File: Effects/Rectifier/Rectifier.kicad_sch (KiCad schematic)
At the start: 36 parts, among them J1 Conn_02x04_Odd_Even, J2 Conn_02x04_Odd_Even, SW1 SW_SPDT, U1 OPA1656, U2 BUF634AxD, U3 OPA1656

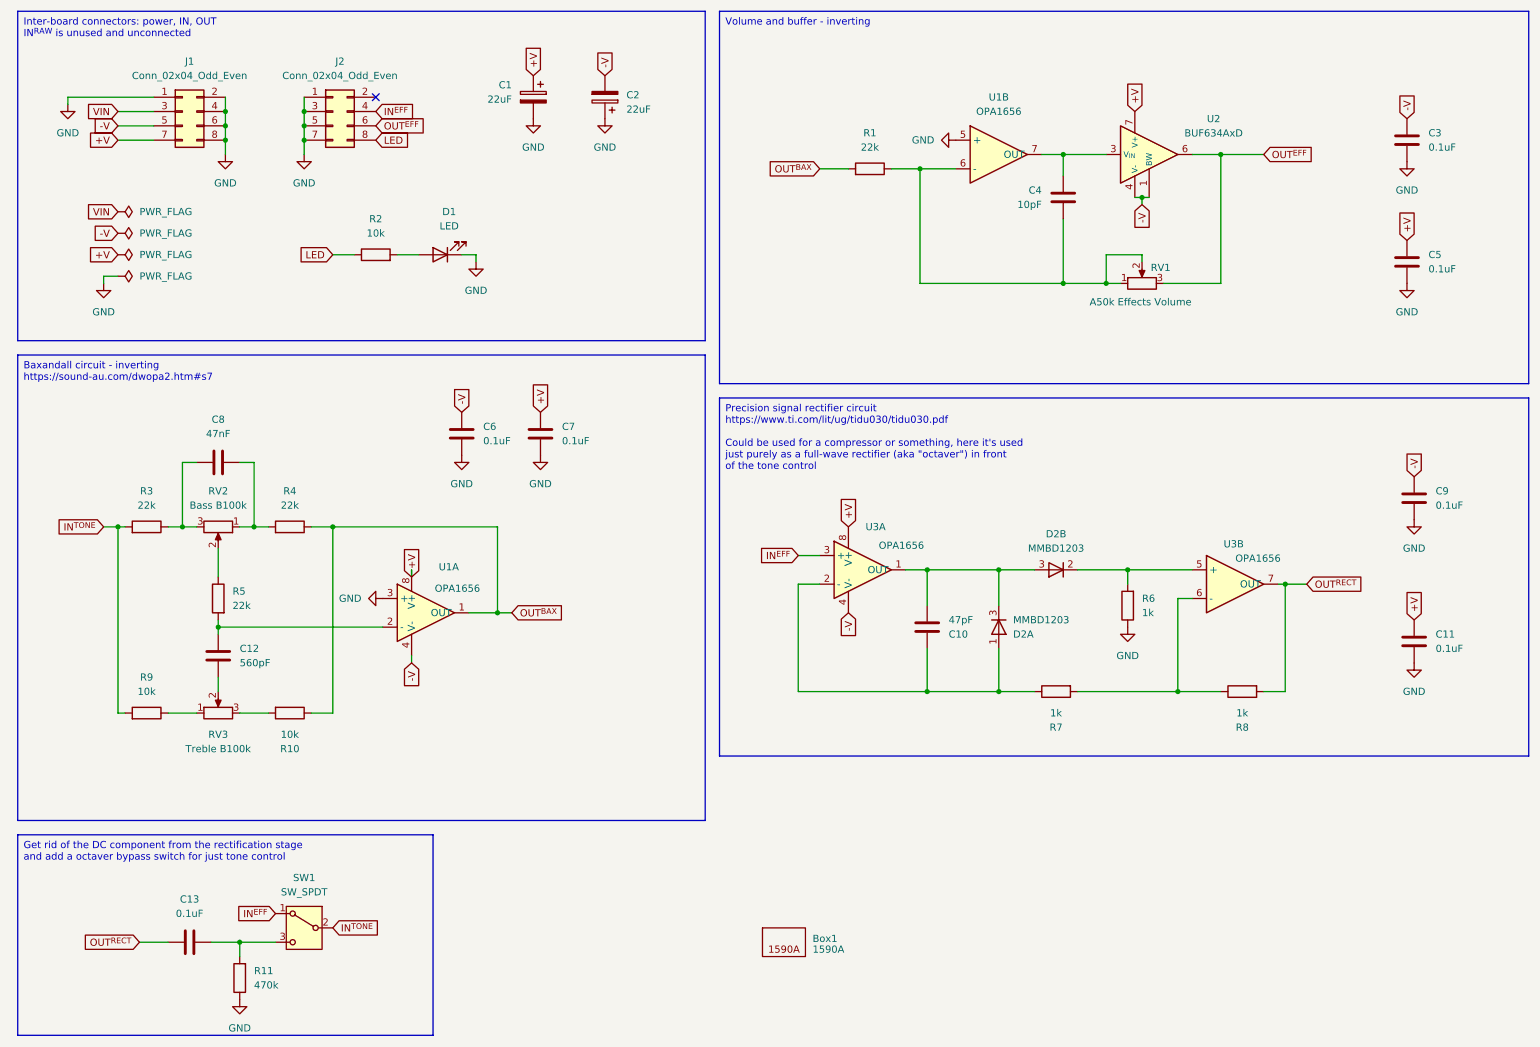
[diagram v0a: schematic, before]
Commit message: Octaver: replace the effect switch with a blending pot
Instead of a hard switch between octaver circuit bypass, use a pot and
another op-amp to blend the original and the rectified signal before the
tone control.

To make it all simpler, this removes the DC bias after blending, so that
the blending inputs are both driven similarly directly from the previous
op-amp.

It shouldn't matter - the blending stage will happily blend in the DC
offset and while it conceptually makes more sense after the
rectification stage rather than the blending stage, the end result is
the same.

Let's hope the end result is "it works". That would be good.

Signed-off-by: Linus Torvalds <torvalds@linux-foundation.org>
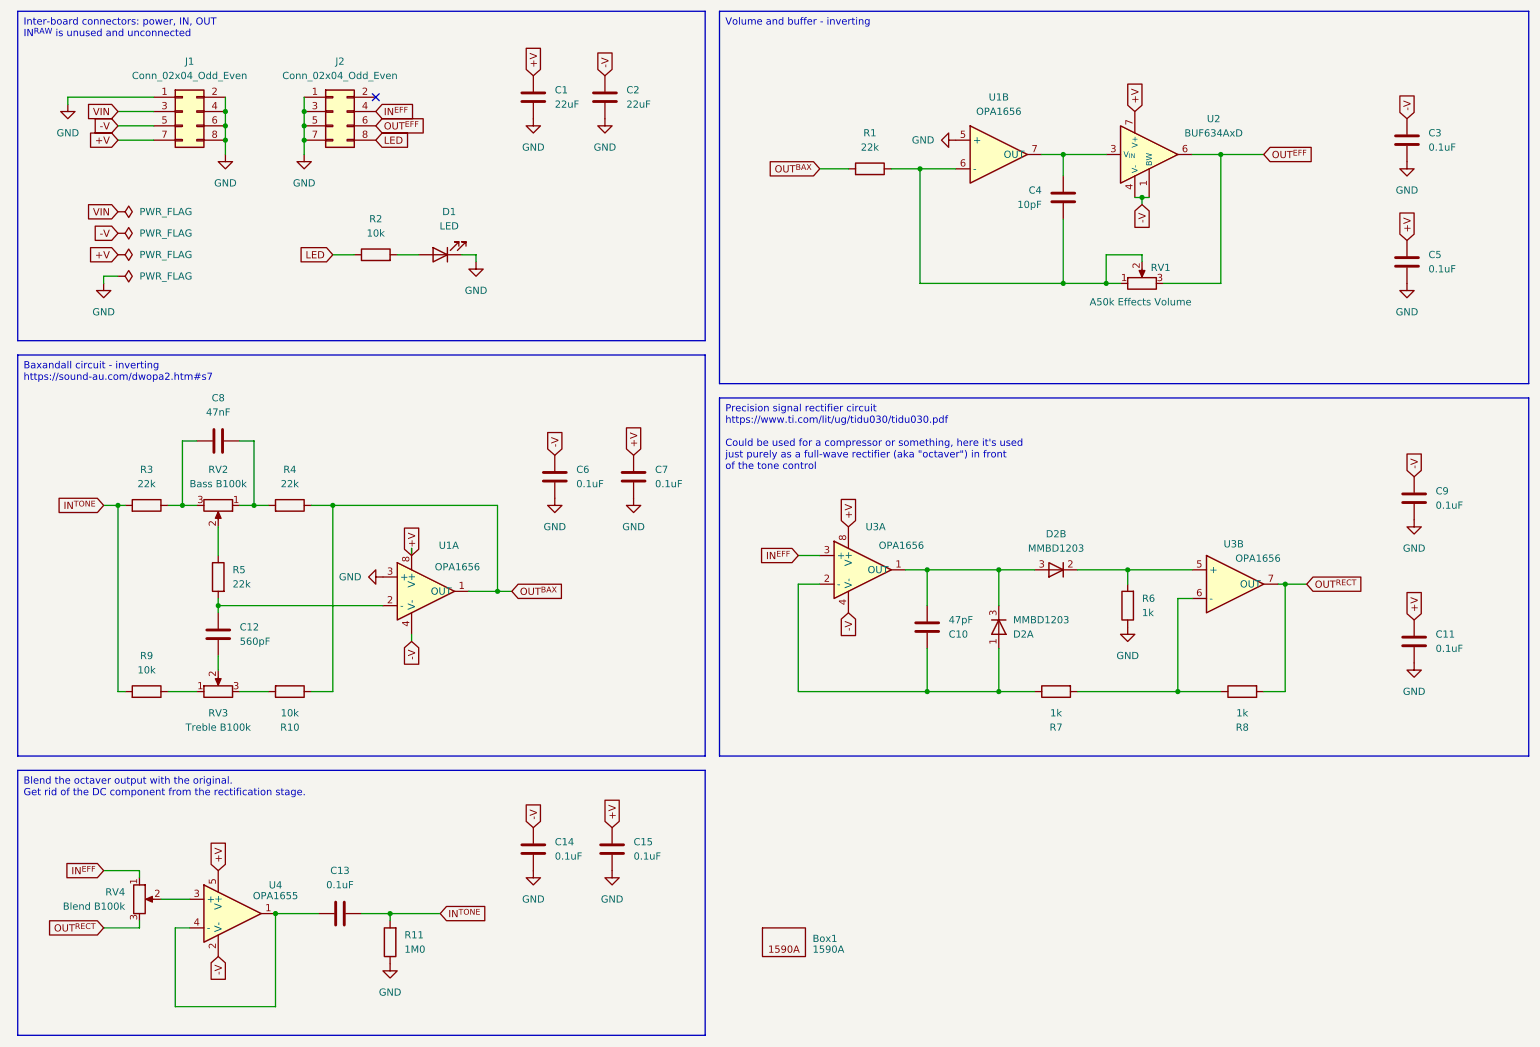
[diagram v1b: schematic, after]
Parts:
- removed C1, C2: 22uF, Capacitor_THT:CP_Radial_D4.0mm_P2.00mm, symbol Device:C_Polarized
- removed SW1: SW_SPDT, Mylib:Tayda Toggle SPDT, symbol Switch:SW_SPDT
- added C1, C2: 22uF, Capacitor_SMD:C_1206_3216Metric_Pad1.33x1.80mm_HandSolder, symbol Device:C
- added C14, C15: 0.1uF, Capacitor_SMD:C_1206_3216Metric_Pad1.33x1.80mm_HandSolder, symbol Device:C
- added RV4: Blend B100k, Potentiometer_THT:Potentiometer_Alpha_RD901F-40-00D_Single_Vertical, symbol Device:R_Potentiometer
- added U4: OPA1655, Package_TO_SOT_SMD:SOT-23-5_HandSoldering, symbol Mylib:OPA1655DVB
- R11: value 470k -> 1M0
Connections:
- net +V: now also C1.1, C15.1, U4.5 (V+)
- net -V: now also C14.1, C2.1, U4.2 (V-)
- net GND: now also C1.2, C14.2, C15.2, C2.2
- net IN^{EFF}: now also RV4.1
- net IN^{TONE}: now also C13.2, R11.2
- net OUT^{RECT}: now also RV4.3; no longer C13.1
- new net: C13.1, U4.1, U4.4 (-)
- new net: RV4.2, U4.3 (+)
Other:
- moved on the sheet: C12, C13, C6, C7, C8, R10, R11, R3, R4, R5, R9, RV2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

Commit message: Convert the USB LDO base board and the Octaver to 2-layer boards
I said I wouldn't do this, because 4-layer boards just makes it easier
being lazy, and doesn't involve messing up the gerbers by switching
stack-up in the middle of the project.

But I wanted to see how painful it would be, particularly with the
fairly packed Octaver board (well, packed for _me_, not like it's
actually all that full).

The inner layers were pretty empty anyway, since I tend to try to avoid
via routing and mainly used them for some power routing, and it really
wasn't that much work.

I've switched to the new smaller Murata caps on these boards at the same
time.

Signed-off-by: Linus Torvalds <torvalds@linux-foundation.org>
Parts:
- C11, C13, C14, C15, C3, C5, C6, C7, C9: footprint Capacitor_SMD:C_1206_3216Metric_Pad1.33x1.80mm_HandSolder -> Mylib:C_0704_1810Metric
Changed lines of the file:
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@@
 			)
 		)
-		(property "Footprint" "Capacitor_SMD:C_1206_3216Metric_Pad1.33x1.80mm_HandSolder"
+		(property "Footprint" "Mylib:C_0704_1810Metric"
 			(at 262.5852 104.14 0)
 			(effects
@@
 			)
 		)
-		(property "Footprint" "Capacitor_SMD:C_1206_3216Metric_Pad1.33x1.80mm_HandSolder"
+		(property "Footprint" "Mylib:C_0704_1810Metric"
 			(at 106.3752 166.37 0)
 			(effects
@@
 			)
 		)
-		(property "Footprint" "Capacitor_SMD:C_1206_3216Metric_Pad1.33x1.80mm_HandSolder"
+		(property "Footprint" "Mylib:C_0704_1810Metric"
 			(at 261.3152 40.64 0)
 			(effects
@@
 			)
 		)
-		(property "Footprint" "Capacitor_SMD:C_1206_3216Metric_Pad1.33x1.80mm_HandSolder"
+		(property "Footprint" "Mylib:C_0704_1810Metric"
 			(at 74.93 173.0248 0)
 			(effects
@@
 			)
 		)
-		(property "Footprint" "Capacitor_SMD:C_1206_3216Metric_Pad1.33x1.80mm_HandSolder"
+		(property "Footprint" "Mylib:C_0704_1810Metric"
 			(at 120.3452 166.37 0)
 			(effects
@@
 			)
 		)
-		(property "Footprint" "Capacitor_SMD:C_1206_3216Metric_Pad1.33x1.80mm_HandSolder"
+		(property "Footprint" "Mylib:C_0704_1810Metric"
 			(at 124.1552 100.33 0)
 			(effects
@@
 			)
 		)
-		(property "Footprint" "Capacitor_SMD:C_1206_3216Metric_Pad1.33x1.80mm_HandSolder"
+		(property "Footprint" "Mylib:C_0704_1810Metric"
 			(at 261.3152 62.23 0)
 			(effects
@@
 			)
 		)
-		(property "Footprint" "Capacitor_SMD:C_1206_3216Metric_Pad1.33x1.80mm_HandSolder"
+		(property "Footprint" "Mylib:C_0704_1810Metric"
 			(at 262.5852 129.54 0)
 			(effects
@@
 			)
 		)
-		(property "Footprint" "Capacitor_SMD:C_1206_3216Metric_Pad1.33x1.80mm_HandSolder"
+		(property "Footprint" "Mylib:C_0704_1810Metric"
 			(at 110.1852 100.33 0)
 			(effects
